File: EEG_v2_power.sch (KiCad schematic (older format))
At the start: 17 parts, among them U2 TLV70033, U3 LM2664, U4 TLV70025, U5 TPS72325

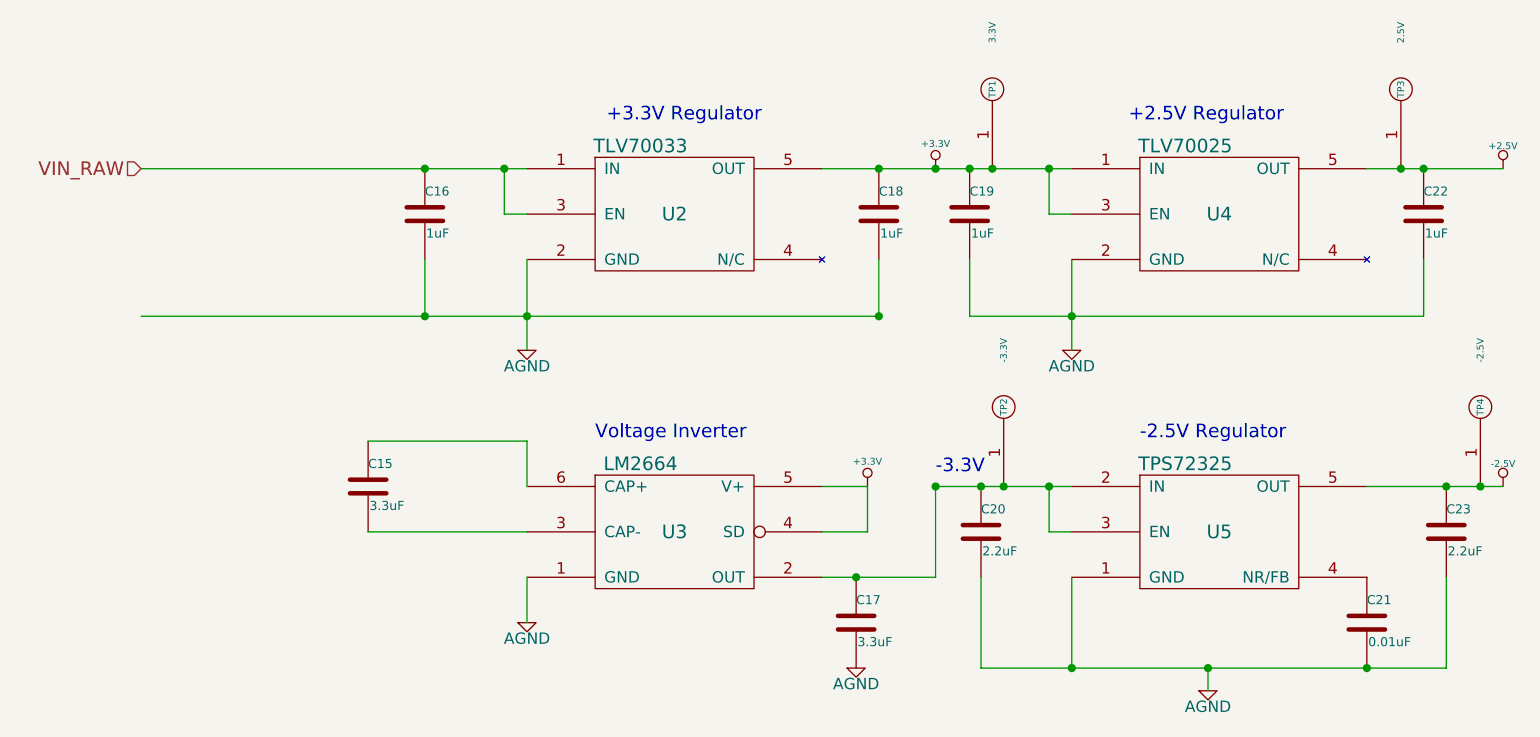
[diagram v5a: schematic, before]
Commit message: Added footprint designators for voltage regulators.
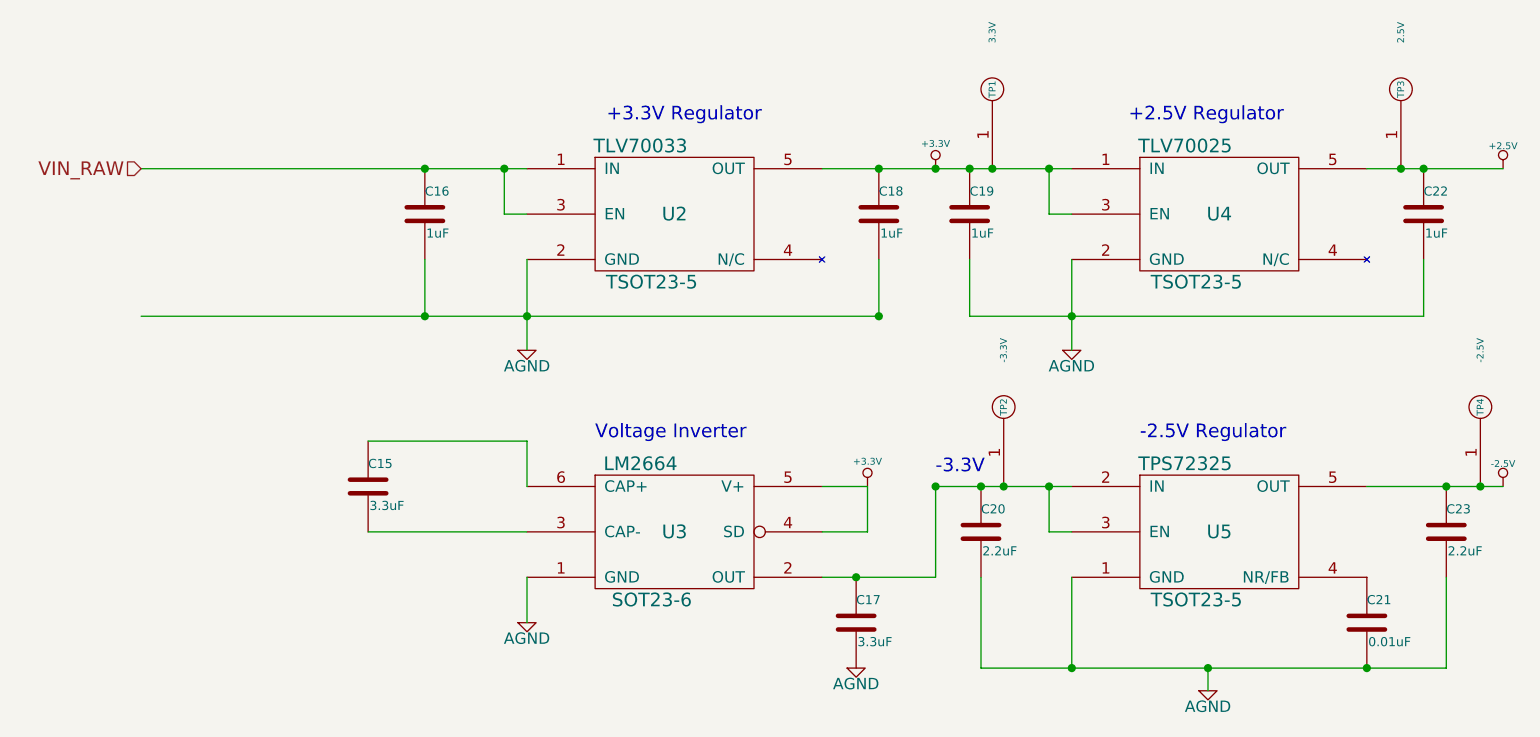
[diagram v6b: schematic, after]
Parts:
- U2, U4, U5: footprint (none) -> TSOT23-5
- U3: footprint (none) -> SOT23-6
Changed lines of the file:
@@
 Sheet 3 4
 Title "Project Synapse Prototype Board"
-Date "28 jan 2015"
+Date "29 jan 2015"
 Rev "A.b"
 Comp "Senior Design 14-15"
@@
 F 0 "U3" H 5300 4650 60  0000 C CNN
 F 1 "LM2664" H 5150 4950 60  0000 C CNN
-F 2 "" H 5300 4650 60  0000 C CNN
+F 2 "SOT23-6" H 5200 4350 60  0000 C CNN
 F 3 "" H 5300 4650 60  0000 C CNN
 	1    5300 4650
@@
 F 0 "U4" H 7700 3250 60  0000 C CNN
 F 1 "TLV70025" H 7550 3550 60  0000 C CNN
-F 2 "" H 7700 3250 60  0000 C CNN
+F 2 "TSOT23-5" H 7600 2950 60  0000 C CNN
 F 3 "" H 7700 3250 60  0000 C CNN
 	1    7700 3250
@@
 F 0 "U2" H 5300 3250 60  0000 C CNN
 F 1 "TLV70033" H 5150 3550 60  0000 C CNN
-F 2 "" H 5300 3250 60  0000 C CNN
+F 2 "TSOT23-5" H 5200 2950 60  0000 C CNN
 F 3 "" H 5300 3250 60  0000 C CNN
 	1    5300 3250
@@
 F 0 "U5" H 7700 4650 60  0000 C CNN
 F 1 "TPS72325" H 7550 4950 60  0000 C CNN
-F 2 "" H 7700 4650 60  0000 C CNN
+F 2 "TSOT23-5" H 7600 4350 60  0000 C CNN
 F 3 "" H 7700 4650 60  0000 C CNN
 	1    7700 4650

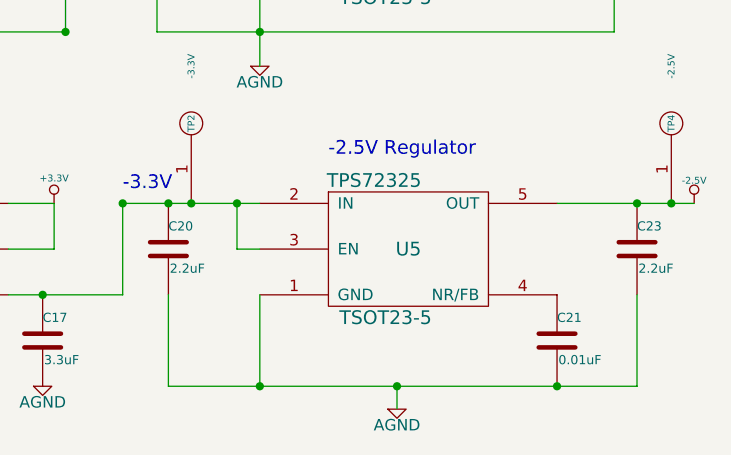
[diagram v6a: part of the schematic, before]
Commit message: Add reset button / jumper
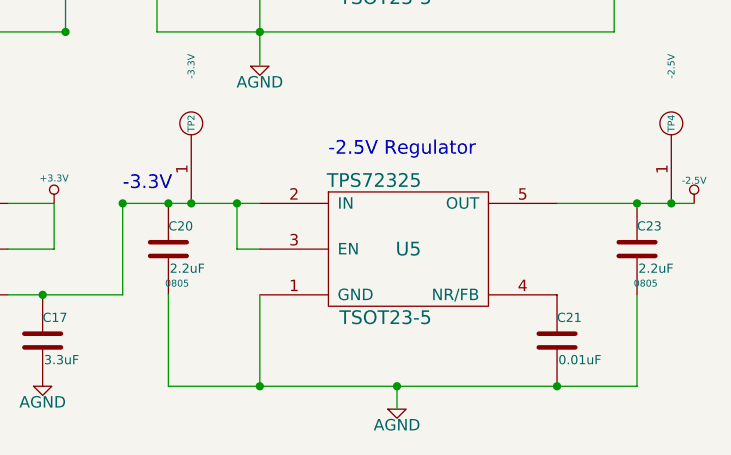
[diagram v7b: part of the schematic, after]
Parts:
- C20, C23: footprint ~ -> 0805
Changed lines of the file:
@@
 F 0 "C20" H 6650 4750 40  0000 L CNN
 F 1 "2.2uF" H 6656 4565 40  0000 L CNN
-F 2 "~" H 6688 4500 30  0000 C CNN
+F 2 "0805" H 6688 4500 30  0000 C CNN
 F 3 "~" H 6650 4650 60  0000 C CNN
 	1    6650 4650
@@
 F 0 "C23" H 8700 4750 40  0000 L CNN
 F 1 "2.2uF" H 8706 4565 40  0000 L CNN
-F 2 "~" H 8738 4500 30  0000 C CNN
+F 2 "0805" H 8738 4500 30  0000 C CNN
 F 3 "~" H 8700 4650 60  0000 C CNN
 	1    8700 4650

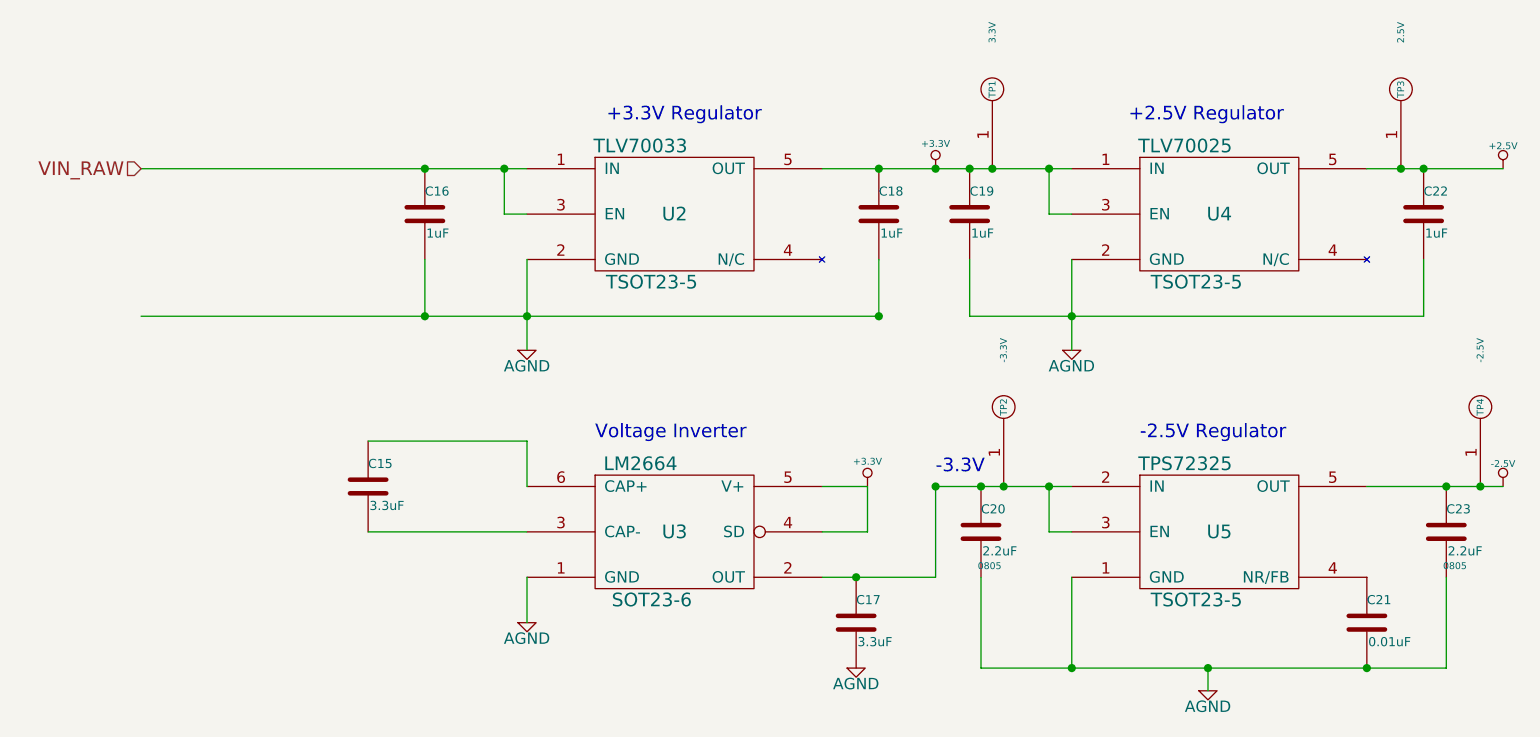
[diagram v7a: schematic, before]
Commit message: Add footprints
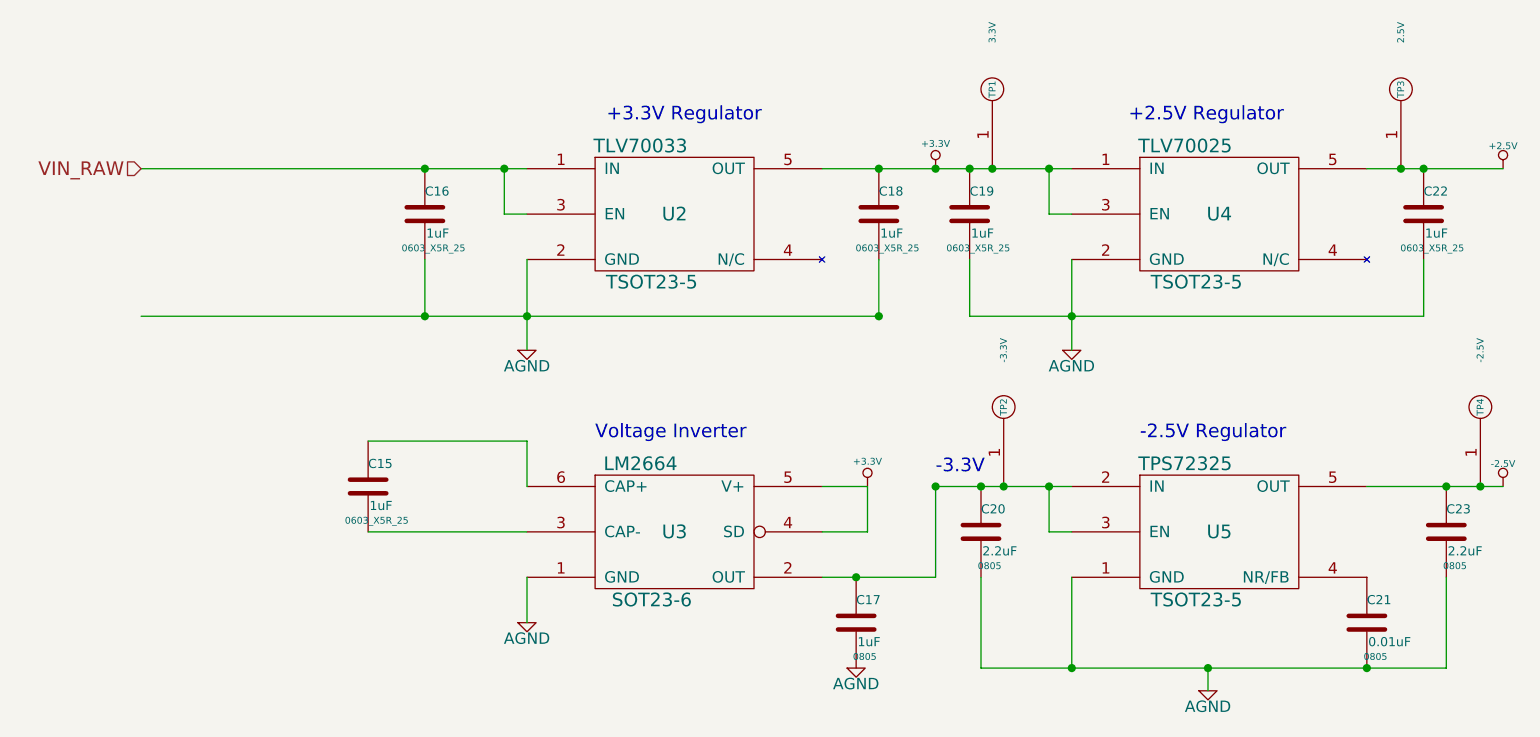
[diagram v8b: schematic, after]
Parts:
- C15: value 3.3uF -> 1uF; footprint ~ -> 0603_X5R_25
- C16, C18, C19, C22: footprint ~ -> 0603_X5R_25
- C17: value 3.3uF -> 1uF; footprint ~ -> 0805
- C21: footprint ~ -> 0805
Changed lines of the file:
@@
 +3.3V Regulator
 $Comp
-L +3.3V #PWR029
+L +3.3V #PWR031
 U 1 1 54B47F4F
 P 6450 3050
-F 0 "#PWR029" H 6450 3010 30  0001 C CNN
+F 0 "#PWR031" H 6450 3010 30  0001 C CNN
 F 1 "+3.3V" H 6450 3160 30  0000 C CNN
 F 2 "~" H 6450 3050 60  0000 C CNN
@@
 $EndComp
 $Comp
-L AGND #PWR030
+L AGND #PWR032
 U 1 1 54B47F55
 P 4650 3850
-F 0 "#PWR030" H 4650 3850 40  0001 C CNN
+F 0 "#PWR032" H 4650 3850 40  0001 C CNN
 F 1 "AGND" H 4650 3780 50  0000 C CNN
 F 2 "~" H 4650 3850 60  0000 C CNN
@@
 F 0 "C16" H 4200 3350 40  0000 L CNN
 F 1 "1uF" H 4206 3165 40  0000 L CNN
-F 2 "~" H 4238 3100 30  0000 C CNN
+F 2 "0603_X5R_25" H 4238 3100 30  0000 C CNN
 F 3 "~" H 4200 3250 60  0000 C CNN
 	1    4200 3250
@@
 F 0 "C18" H 6200 3350 40  0000 L CNN
 F 1 "1uF" H 6206 3165 40  0000 L CNN
-F 2 "~" H 6238 3100 30  0000 C CNN
+F 2 "0603_X5R_25" H 6238 3100 30  0000 C CNN
 F 3 "~" H 6200 3250 60  0000 C CNN
 	1    6200 3250
@@
 F 0 "C19" H 6600 3350 40  0000 L CNN
 F 1 "1uF" H 6606 3165 40  0000 L CNN
-F 2 "~" H 6638 3100 30  0000 C CNN
+F 2 "0603_X5R_25" H 6638 3100 30  0000 C CNN
 F 3 "~" H 6600 3250 60  0000 C CNN
 	1    6600 3250
@@
 $EndComp
 $Comp
-L AGND #PWR031
+L AGND #PWR033
 U 1 1 54B47F6D
 P 7050 3850
-F 0 "#PWR031" H 7050 3850 40  0001 C CNN
+F 0 "#PWR033" H 7050 3850 40  0001 C CNN
 F 1 "AGND" H 7050 3780 50  0000 C CNN
 F 2 "~" H 7050 3850 60  0000 C CNN
@@
 F 0 "C22" H 8600 3350 40  0000 L CNN
 F 1 "1uF" H 8606 3165 40  0000 L CNN
-F 2 "~" H 8638 3100 30  0000 C CNN
+F 2 "0603_X5R_25" H 8638 3100 30  0000 C CNN
 F 3 "~" H 8600 3250 60  0000 C CNN
 	1    8600 3250
@@
 $EndComp
 $Comp
-L +2.5V #PWR032
+L +2.5V #PWR034
 U 1 1 54B47F79
 P 8950 3050
-F 0 "#PWR032" H 8950 3000 20  0001 C CNN
+F 0 "#PWR034" H 8950 3000 20  0001 C CNN
 F 1 "+2.5V" H 8950 3150 30  0000 C CNN
 F 2 "" H 8950 3050 60  0000 C CNN
@@
 P 3950 4450
 F 0 "C15" H 3950 4550 40  0000 L CNN
-F 1 "3.3uF" H 3956 4365 40  0000 L CNN
-F 2 "~" H 3988 4300 30  0000 C CNN
+F 1 "1uF" H 3956 4365 40  0000 L CNN
+F 2 "0603_X5R_25" H 3988 4300 30  0000 C CNN
 F 3 "~" H 3950 4450 60  0000 C CNN
 	1    3950 4450
@@
 $EndComp
 $Comp
-L AGND #PWR033
+L AGND #PWR035
 U 1 1 54B47F86
 P 4650 5050
-F 0 "#PWR033" H 4650 5050 40  0001 C CNN
+F 0 "#PWR035" H 4650 5050 40  0001 C CNN
 F 1 "AGND" H 4650 4980 50  0000 C CNN
 F 2 "~" H 4650 5050 60  0000 C CNN
@@
 P 6100 5050
 F 0 "C17" H 6100 5150 40  0000 L CNN
-F 1 "3.3uF" H 6106 4965 40  0000 L CNN
-F 2 "~" H 6138 4900 30  0000 C CNN
+F 1 "1uF" H 6106 4965 40  0000 L CNN
+F 2 "0805" H 6138 4900 30  0000 C CNN
 F 3 "~" H 6100 5050 60  0000 C CNN
 	1    6100 5050
@@
 $EndComp
 $Comp
-L AGND #PWR034
+L AGND #PWR036
 U 1 1 54B47F92
 P 6100 5250
-F 0 "#PWR034" H 6100 5250 40  0001 C CNN
+F 0 "#PWR036" H 6100 5250 40  0001 C CNN
 F 1 "AGND" H 6100 5180 50  0000 C CNN
 F 2 "~" H 6100 5250 60  0000 C CNN
@@
 $EndComp
 $Comp
-L +3.3V #PWR035
+L +3.3V #PWR037
 U 1 1 54B47F98
 P 6150 4450
-F 0 "#PWR035" H 6150 4410 30  0001 C CNN
+F 0 "#PWR037" H 6150 4410 30  0001 C CNN
 F 1 "+3.3V" H 6150 4560 30  0000 C CNN
 F 2 "~" H 6150 4450 60  0000 C CNN
@@
 F 0 "C21" H 8350 5150 40  0000 L CNN
 F 1 "0.01uF" H 8356 4965 40  0000 L CNN
-F 2 "~" H 8388 4900 30  0000 C CNN
+F 2 "0805" H 8388 4900 30  0000 C CNN
 F 3 "~" H 8350 5050 60  0000 C CNN
 	1    8350 5050
@@
 $EndComp
 $Comp
-L AGND #PWR036
+L AGND #PWR038
 U 1 1 54B47FB2
 P 7650 5350
-F 0 "#PWR036" H 7650 5350 40  0001 C CNN
+F 0 "#PWR038" H 7650 5350 40  0001 C CNN
 F 1 "AGND" H 7650 5280 50  0000 C CNN
 F 2 "~" H 7650 5350 60  0000 C CNN
@@
 $EndComp
 $Comp
-L -2.5V #PWR037
+L -2.5V #PWR039
 U 1 1 54B47FB8
 P 8950 4450
-F 0 "#PWR037" H 8950 4400 20  0001 C CNN
+F 0 "#PWR039" H 8950 4400 20  0001 C CNN
 F 1 "-2.5V" H 8950 4550 30  0000 C CNN
 F 2 "" H 8950 4450 60  0000 C CNN
